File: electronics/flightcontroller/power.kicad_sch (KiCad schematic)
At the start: 20 parts, among them J1 BATT, U1 DS2745U, U4 MIC5514-3.3, U5 AOZ6663DI

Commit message: electronics: Draft most of the flight controller schematics.
The power supply part is not complete, and all connections to the MCU are
missing.
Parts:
- R2: Mouser (none) -> 71-WSL06121L000FEA
- U1: Digikey (none) -> DS2745U+CT-ND; Mouser (none) -> DS2745U+T&R
- U4: Mouser (none) -> 998-MIC5514-3.3YMTTR
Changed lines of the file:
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@@
+      (effects (font (size 1.27 1.27)) hide)
+    )
+    (property "Mouser" "71-WSL06121L000FEA" (id 5) (at 54.61 93.98 90)
       (effects (font (size 1.27 1.27)) hide)
     )
@@
     )
     (property "Digikey" "576-4433-1-ND" (id 4) (at 242.57 72.39 0)
+      (effects (font (size 1.27 1.27)) hide)
+    )
+    (property "Mouser" "998-MIC5514-3.3YMTTR" (id 5) (at 242.57 72.39 0)
       (effects (font (size 1.27 1.27)) hide)
     )
@@
       (effects (font (size 1.27 1.27)) hide)
     )
+    (property "Digikey" "DS2745U+CT-ND" (id 4) (at 76.2 81.28 0)
+      (effects (font (size 1.27 1.27)) hide)
+    )
+    (property "Mouser" "DS2745U+T&R" (id 5) (at 76.2 81.28 0)
+      (effects (font (size 1.27 1.27)) hide)
+    )

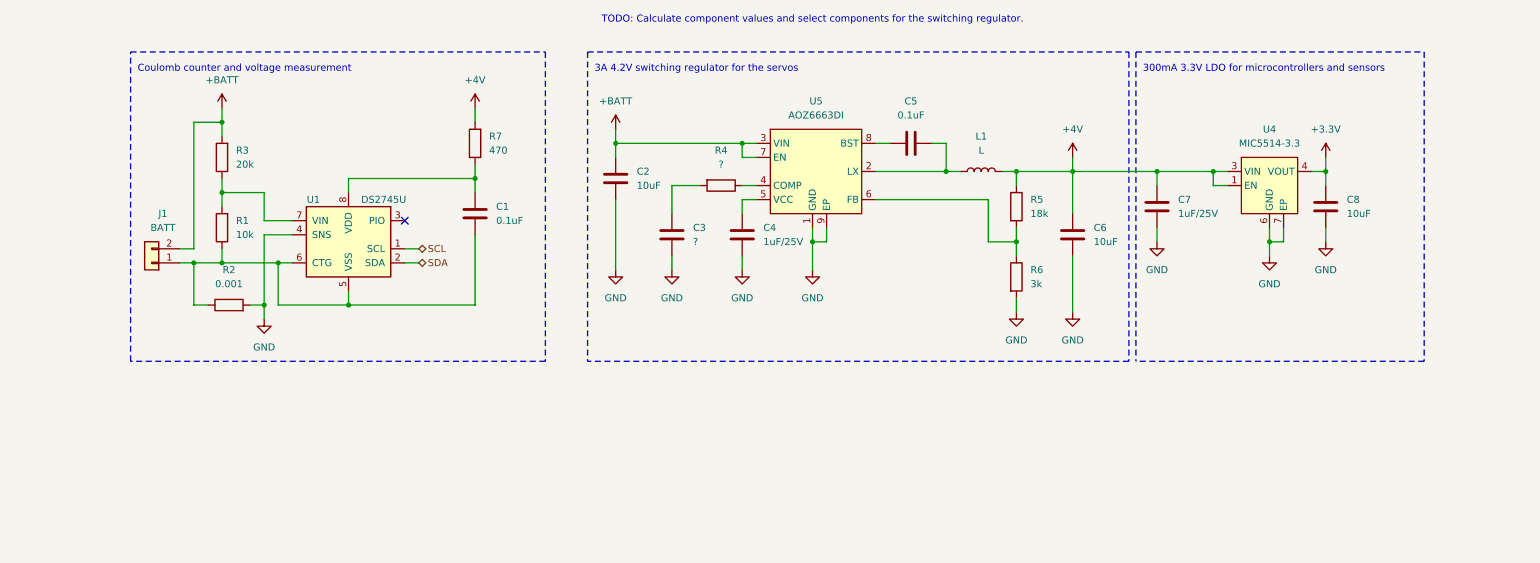
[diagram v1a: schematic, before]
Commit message: electronics: Changed the 4V regulator and added some ordering codes.
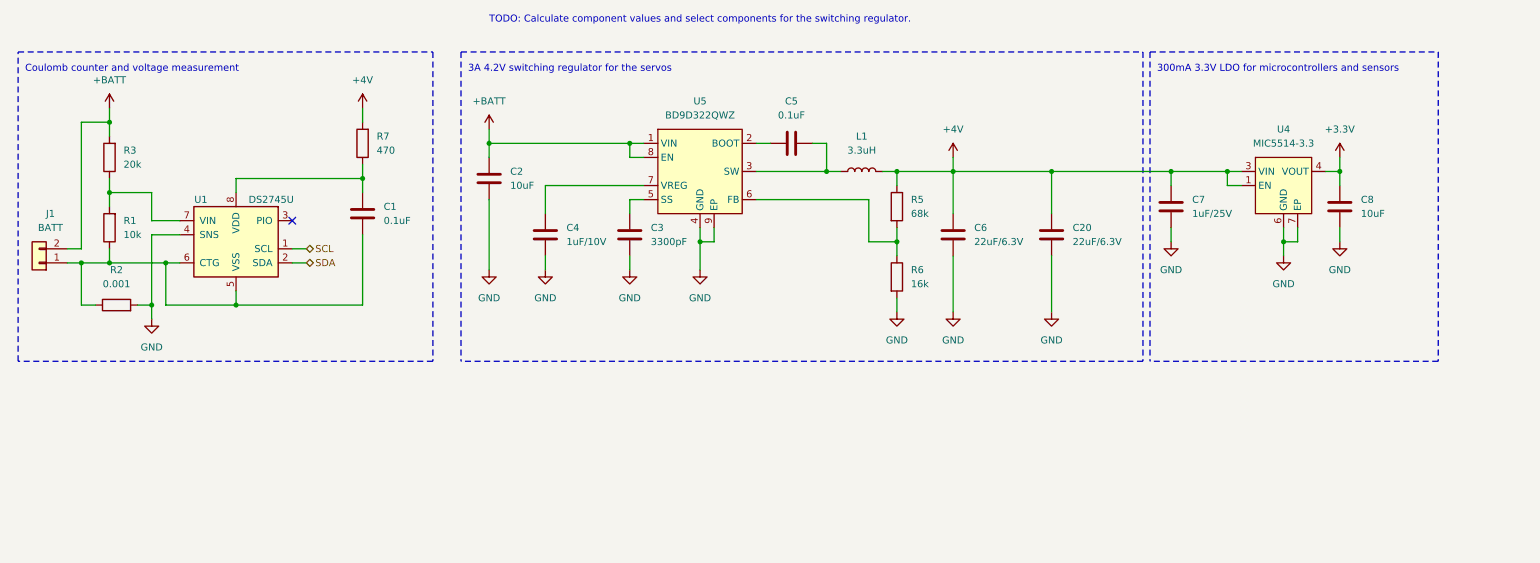
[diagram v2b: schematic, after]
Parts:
- removed R4: ?, Resistor_SMD:R_0402_1005Metric, symbol Device:R
- removed U5: AOZ6663DI, flightcontroller-footprints:DFN-6-1EP_3x3mm_P0.65mm_EP1.25x2.7mm, symbol flightcontroller-symbols:AOZ6663DI
- added C20: 22uF/6.3V, Capacitor_SMD:C_0805_2012Metric, symbol Device:C
- added U5: BD9D322QWZ, symbol flightcontroller-symbols:BD9D322QWZ
- C1, C5: Mouser (none) -> 81-GRM155R61H104KE4D
- C3: value ? -> 3300pF; Digikey (none) -> 587-6368-1-ND; Mouser (none) -> 963-UMK105BJ332KV-F
- C4: value 1uF/25V -> 1uF/10V; footprint Capacitor_SMD:C_0603_1608Metric -> Capacitor_SMD:C_0402_1005Metric; Digikey 1276-1184-1-ND -> 1276-1067-1-ND; Mouser (none) -> 963-LMK105BJ105MVHF
- C6: value 10uF -> 22uF/6.3V; Digikey 587-6025-1-ND -> 445-7663-1-ND
- L1: value L -> 3.3uH; Digikey (none) -> 478-LMLP0506M3R3DTASCT-ND; Mouser (none) -> 581-LMLP0506M3R3DTAS
- R5: value 18k -> 68k
- R6: value 3k -> 16k
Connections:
- net +4V: now also C20.2
- net +BATT: now also U5.1 (VIN), U5.8 (EN)
- net GND: now also C20.1, U5.4 (GND), U5.9 (EP)
- net at R5.2, R6.1: now also U5.6 (FB)
- net at C5.2, L1.1: now also U5.3 (SW)
- net at C4.1: now also U5.7 (VREG)
- net at C5.1: now also U5.2 (BOOT)
- net at C3.1: now also U5.5 (SS)
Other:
- moved on the sheet: C1, C2, C3, C4, C5, C6, C7, C8, J1, L1, R1, R2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

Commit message: PCB: USB, micro SD, and many component changes.
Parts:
- C1, C5: Mouser 81-GRM155R61H104KE4D -> 81-GRM155R71H104KE4D
- C2: value 10uF -> 10uF/25V; Digikey 587-6025-1-ND -> (none); Mouser (none) -> 187-CL21A106KAYNNNG
- C20, C6: Digikey 445-7663-1-ND -> (none); Mouser (none) -> 187-CL21A226MQQNNNG
- C3: Digikey 587-6368-1-ND -> (none); Mouser 963-UMK105BJ332KV-F -> 81-GCM155R71H332KA7J
- C4: value 1uF/10V -> 1uF/10V; Digikey 1276-1067-1-ND -> (none); Mouser 963-LMK105BJ105MVHF -> 81-GRM155R61E105MA2D
- C7: value 1uF/25V -> 1uF/25V; footprint Capacitor_SMD:C_0603_1608Metric -> Capacitor_SMD:C_0402_1005Metric; Digikey 1276-1184-1-ND -> (none); Mouser (none) -> 81-GRM155R61E105MA2D
- C8: value 10uF -> 10uF/6.3V; footprint Capacitor_SMD:C_0805_2012Metric -> Capacitor_SMD:C_0402_1005Metric; Digikey 587-6025-1-ND -> (none); Mouser (none) -> 81-GRM155R60J106M05D
- L1: footprint (none) -> flightcontroller-footprints:L_AVX_LMLP0506D
- R2: footprint Resistor_SMD:R_0612_1632Metric -> Resistor_SMD:R_2512_6332Metric; Digikey CRK0612-FZ-R001ECT-ND -> (none); Mouser 71-WSL06121L000FEA -> 66-ULRB2R001FLFSLT
- U5: footprint (none) -> flightcontroller-footprints:Rohm_BD9D322QWZ
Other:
- moved on the sheet: C20, C3, C4, C5, C6, C7, C8, L1, R5, R6, U4, U5

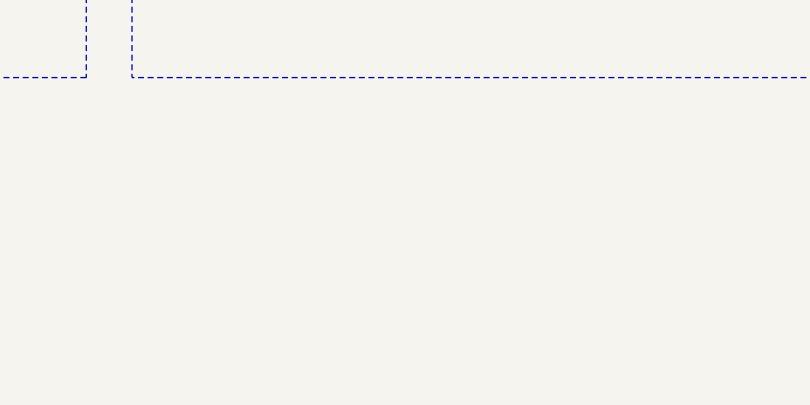
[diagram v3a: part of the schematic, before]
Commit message: electronics: Microcontroller connections, general component placement.
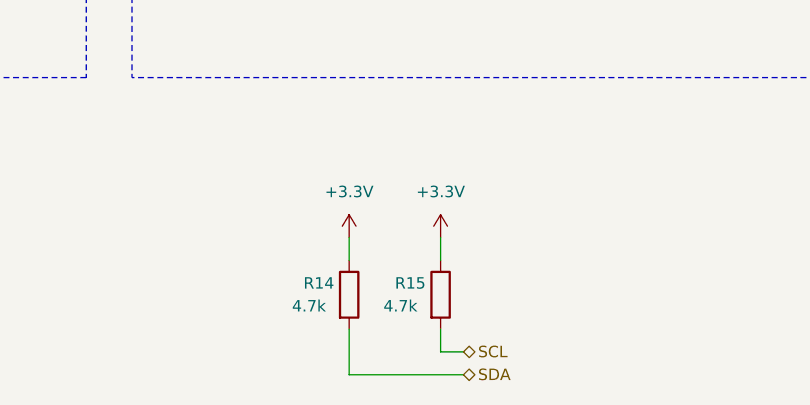
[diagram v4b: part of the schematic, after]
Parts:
- added R14, R15: 4.7k, Resistor_SMD:R_0402_1005Metric, symbol Device:R
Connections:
- net +3V3: now also R14.1, R15.1
- net SCL: now also R15.2
- net SDA: now also R14.2
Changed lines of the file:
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@@
+    (stroke (width 0) (type solid) (color 0 0 0 0))
+  )
+  (wire (pts (xy 120.65 121.92) (xy 120.65 124.46))
+    (stroke (width 0) (type solid) (color 0 0 0 0))
+  )
+  (wire (pts (xy 120.65 137.16) (xy 120.65 132.08))
+    (stroke (width 0) (type solid) (color 0 0 0 0))
+  )
+  (wire (pts (xy 130.81 121.92) (xy 130.81 124.46))
+    (stroke (width 0) (type solid) (color 0 0 0 0))
+  )
+  (wire (pts (xy 130.81 134.62) (xy 130.81 132.08))
     (stroke (width 0) (type solid) (color 0 0 0 0))
   )
@@
   )
   (wire (pts (xy 132.08 85.09) (xy 132.08 87.63))
+    (stroke (width 0) (type solid) (color 0 0 0 0))
+  )
+  (wire (pts (xy 133.35 134.62) (xy 130.81 134.62))
+    (stroke (width 0) (type solid) (color 0 0 0 0))
+  )
+  (wire (pts (xy 133.35 137.16) (xy 120.65 137.16))
     (stroke (width 0) (type solid) (color 0 0 0 0))
   )
@@
     (effects (font (size 1.27 1.27)) (justify left))
   )
+  (hierarchical_label "SCL" (shape bidirectional) (at 133.35 134.62 0)
+    (effects (font (size 1.27 1.27)) (justify left))
+  )
+  (hierarchical_label "SDA" (shape bidirectional) (at 133.35 137.16 0)
+    (effects (font (size 1.27 1.27)) (justify left))
+  )
   (symbol (lib_id "power:+BATT") (at 33.02 58.42 0) (unit 1)
     (in_bom yes) (on_board yes) (fields_autoplaced)
@@
     )
     (property "Datasheet" "" (id 3) (at 101.6 62.23 0)
+      (effects (font (size 1.27 1.27)) hide)
+    )
+    (pin "1")
+  )
+  (symbol (lib_id "power:+3.3V") (at 120.65 121.92 0) (unit 1)
+    (in_bom yes) (on_board yes) (fields_autoplaced)
+    (property "Reference" "#PWR018" (id 0) (at 120.65 125.73 0)
+      (effects (font (size 1.27 1.27)) hide)
+    )
+    (property "Value" "+3.3V" (id 1) (at 120.65 116.84 0))
+    (property "Footprint" "" (id 2) (at 120.65 121.92 0)
+      (effects (font (size 1.27 1.27)) hide)
+    )
+    (property "Datasheet" "" (id 3) (at 120.65 121.92 0)
+      (effects (font (size 1.27 1.27)) hide)
+    )
+    (pin "1")
+  )
+  (symbol (lib_id "power:+3.3V") (at 130.81 121.92 0) (unit 1)
+    (in_bom yes) (on_board yes) (fields_autoplaced)
+    (property "Reference" "#PWR019" (id 0) (at 130.81 125.73 0)
+      (effects (font (size 1.27 1.27)) hide)
+    )
+    (property "Value" "+3.3V" (id 1) (at 130.81 116.84 0))
+    (property "Footprint" "" (id 2) (at 130.81 121.92 0)
+      (effects (font (size 1.27 1.27)) hide)
+    )
+    (property "Datasheet" "" (id 3) (at 130.81 121.92 0)
       (effects (font (size 1.27 1.27)) hide)
     )
@@
       (effects (font (size 1.27 1.27)) hide)
     )
+    (pin "1")
+    (pin "2")
+  )
+  (symbol (lib_id "Device:R") (at 120.65 128.27 0) (unit 1)
+    (in_bom yes) (on_board yes)
+    (property "Reference" "R14" (id 0) (at 115.57 126.9999 0)
+      (effects (font (size 1.27 1.27)) (justify left))
+    )
+    (property "Value" "4.7k" (id 1) (at 114.3 129.5399 0)
+      (effects (font (size 1.27 1.27)) (justify left))
+    )
+    (property "Footprint" "Resistor_SMD:R_0402_1005Metric" (id 2) (at 118.872 128.27 90)
+      (effects (font (size 1.27 1.27)) hide)
+    )
+    (property "Datasheet" "~" (id 3) (at 120.65 128.27 0)
+      (effects (font (size 1.27 1.27)) hide)
+    )
+    (pin "1")
+    (pin "2")
+  )
+  (symbol (lib_id "Device:R") (at 130.81 128.27 0) (unit 1)
+    (in_bom yes) (on_board yes)
+    (property "Reference" "R15" (id 0) (at 125.73 126.9999 0)
+      (effects (font (size 1.27 1.27)) (justify left))
+    )
+    (property "Value" "4.7k" (id 1) (at 124.46 129.5399 0)
+      (effects (font (size 1.27 1.27)) (justify left))
+    )
+    (property "Footprint" "Resistor_SMD:R_0402_1005Metric" (id 2) (at 129.032 128.27 90)
+      (effects (font (size 1.27 1.27)) hide)
+    )
+    (property "Datasheet" "~" (id 3) (at 130.81 128.27 0)
+      (effects (font (size 1.27 1.27)) hide)
+    )

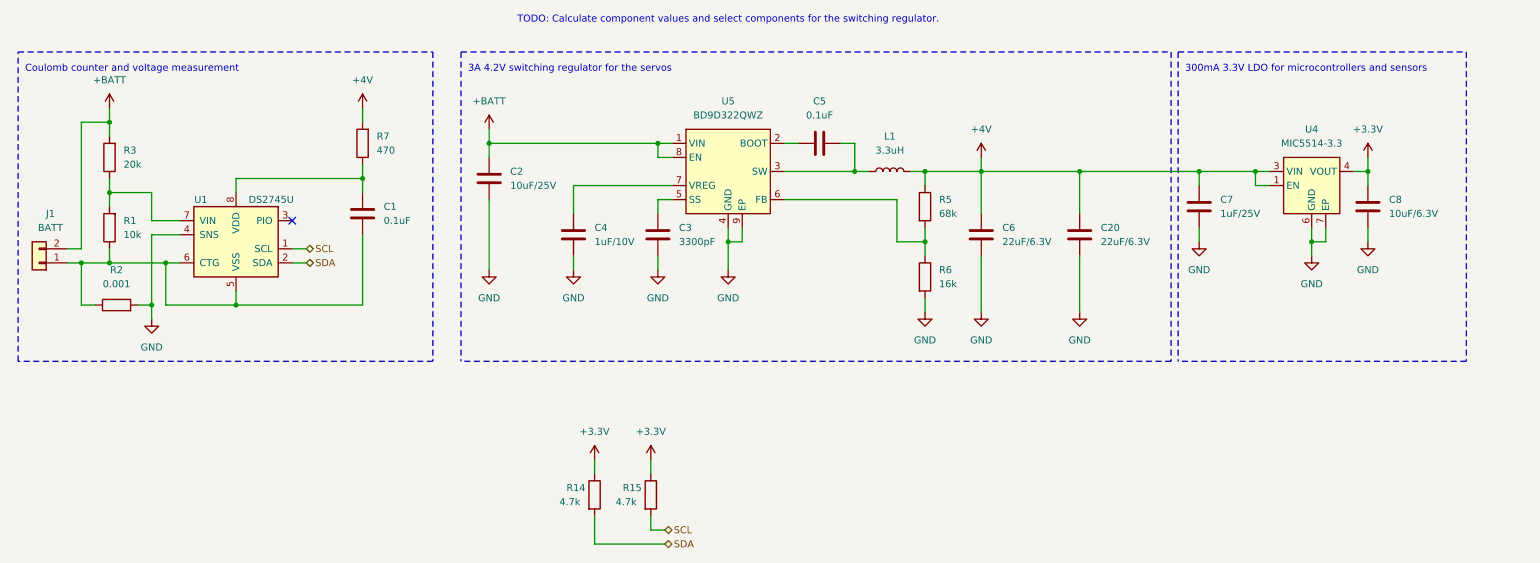
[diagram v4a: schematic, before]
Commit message: electronics: Fix remaining schematics ERC errors.
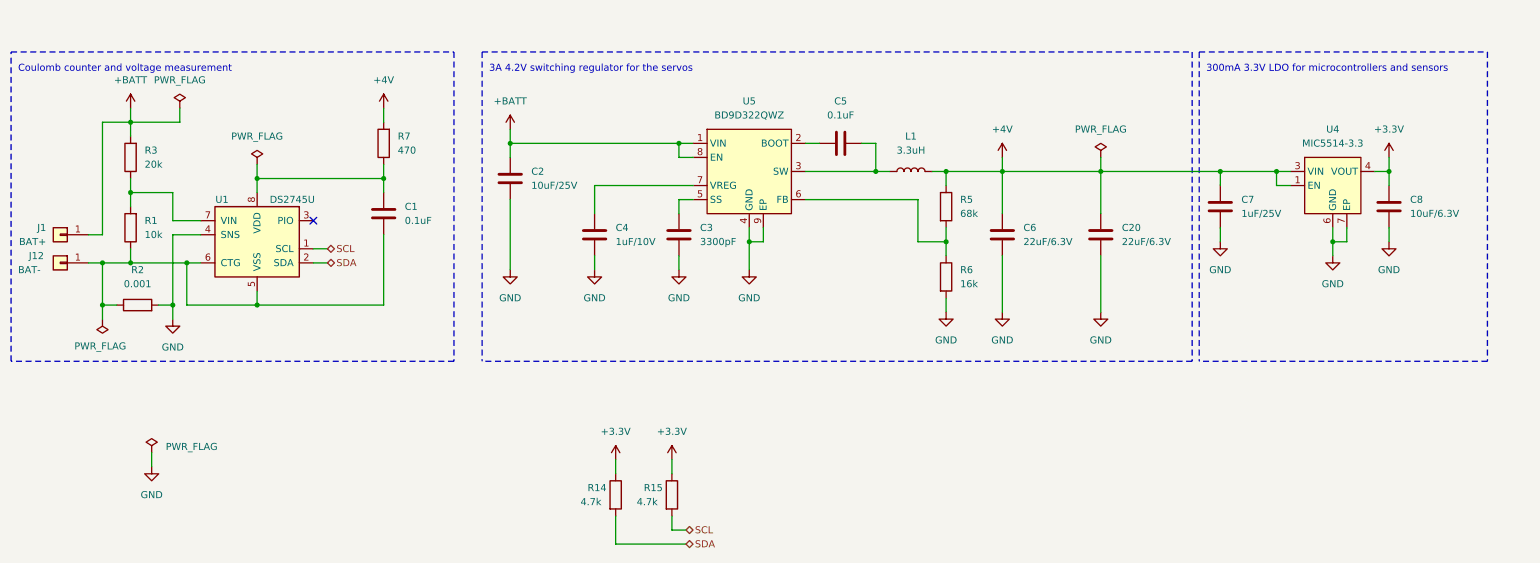
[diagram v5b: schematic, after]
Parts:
- removed J1: BATT, Connector_AMASS:AMASS_XT30U-F_1x02_P5.0mm_Vertical, symbol Connector_Generic:Conn_01x02
- added J1: BAT+, TestPoint:TestPoint_Pad_4.0x4.0mm, symbol Connector_Generic:Conn_01x01
- added J12: BAT-, TestPoint:TestPoint_Pad_4.0x4.0mm, symbol Connector_Generic:Conn_01x01
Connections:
- net +BATT: now also J1.1 (Pin_1)
- net at U4.2 (NC): no longer U4.5 (NC)
- net at C1.2, R1.1, R2.1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: now also J12.1 (Pin_1)
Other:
- note removed: "TODO: Calculate component values and select components for the switching regulator."
- moved on the sheet: C1, C2, C20, C3, C4, C5, C6, C7, C8, L1, R1, R14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

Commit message: electronics: Finished wiring of the flight controller PCB.
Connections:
- net -BATT: now reaches C1.2, J12.1 (Pin_1), R1.1, R2.1, U1.5 (VSS), U1.6 (CTG)
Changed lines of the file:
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@@
   (junction (at 264.16 69.85) (diameter 0.9144) (color 0 0 0 0))
   (no_connect (at 69.85 78.74))
+  (wire (pts (xy 25.4 93.98) (xy 31.75 93.98))
+    (stroke (width 0) (type solid) (color 0 0 0 0))
+  )
   (wire (pts (xy 29.21 81.28) (xy 31.75 81.28))
     (stroke (width 0) (type solid) (color 0 0 0 0))
@@
     (effects (font (size 1.27 1.27)) (justify left bottom))
   )
+  (label "-BATT" (at 25.4 93.98 0)
+    (effects (font (size 1.27 1.27)) (justify left bottom))
+  )
